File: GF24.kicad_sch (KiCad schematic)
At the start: 52 parts, among them J1 Conn_02x05_Odd_Even, J2 USB_C_Receptacle_PowerOnly_6P, Q1 MMBT3904LT1G, SW1 NRST, SW2 SW_Nidec_CAS-120A1, SW3 NRST, SW4 ON/OFF, SW5 MODE, U1 STM32F031C4T6, U2 SAM-M10Q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

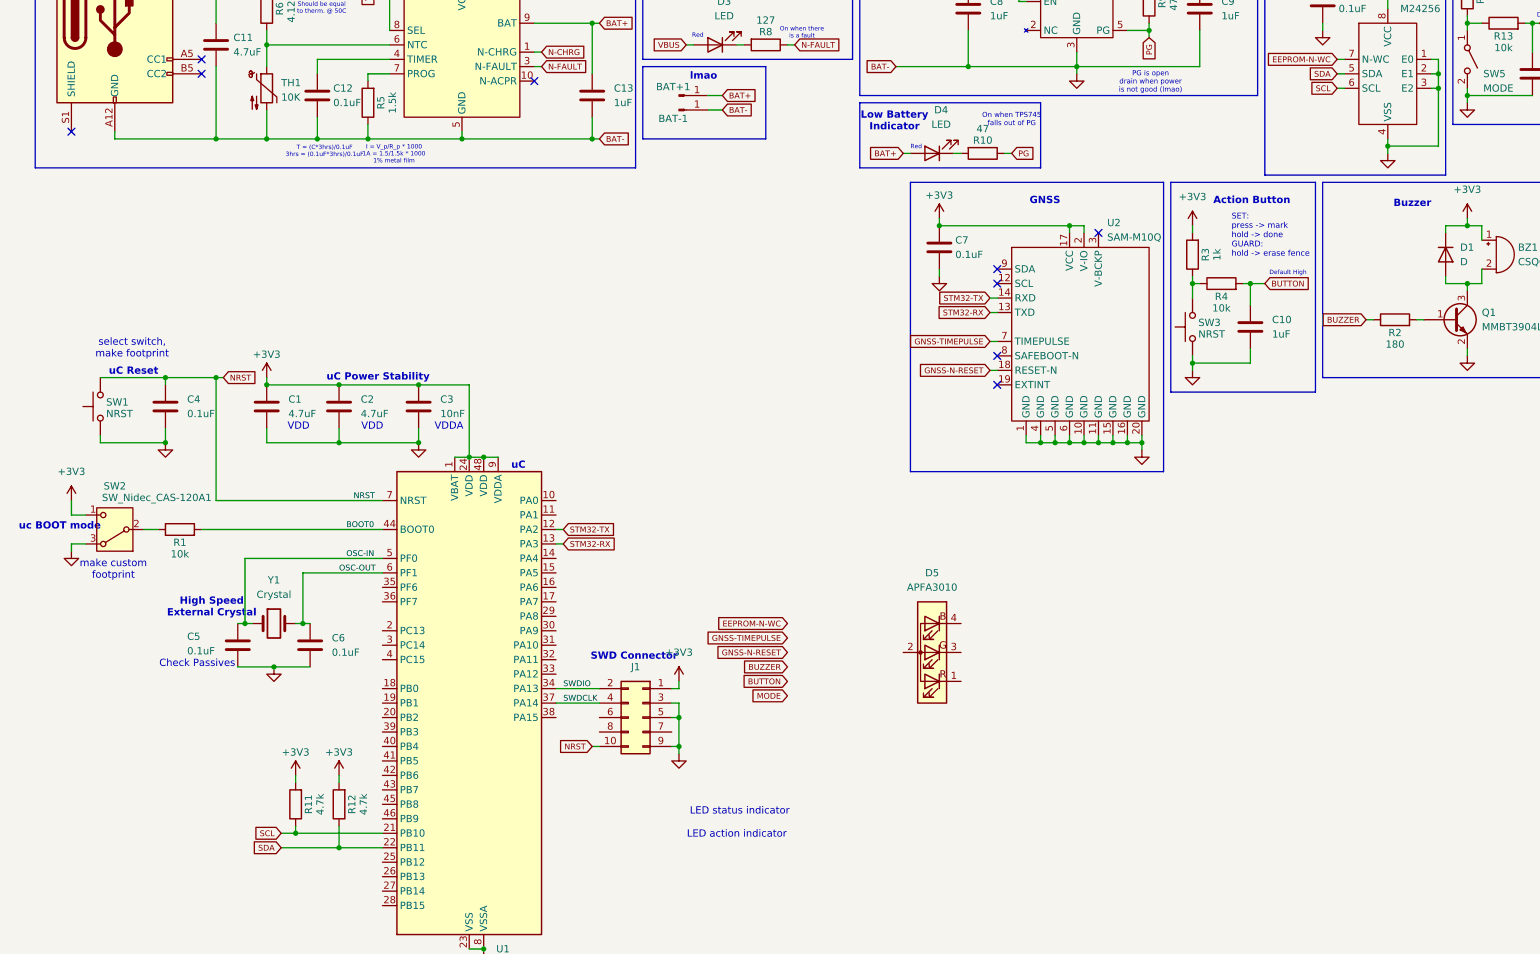
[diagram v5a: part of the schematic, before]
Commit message: added status LEDs
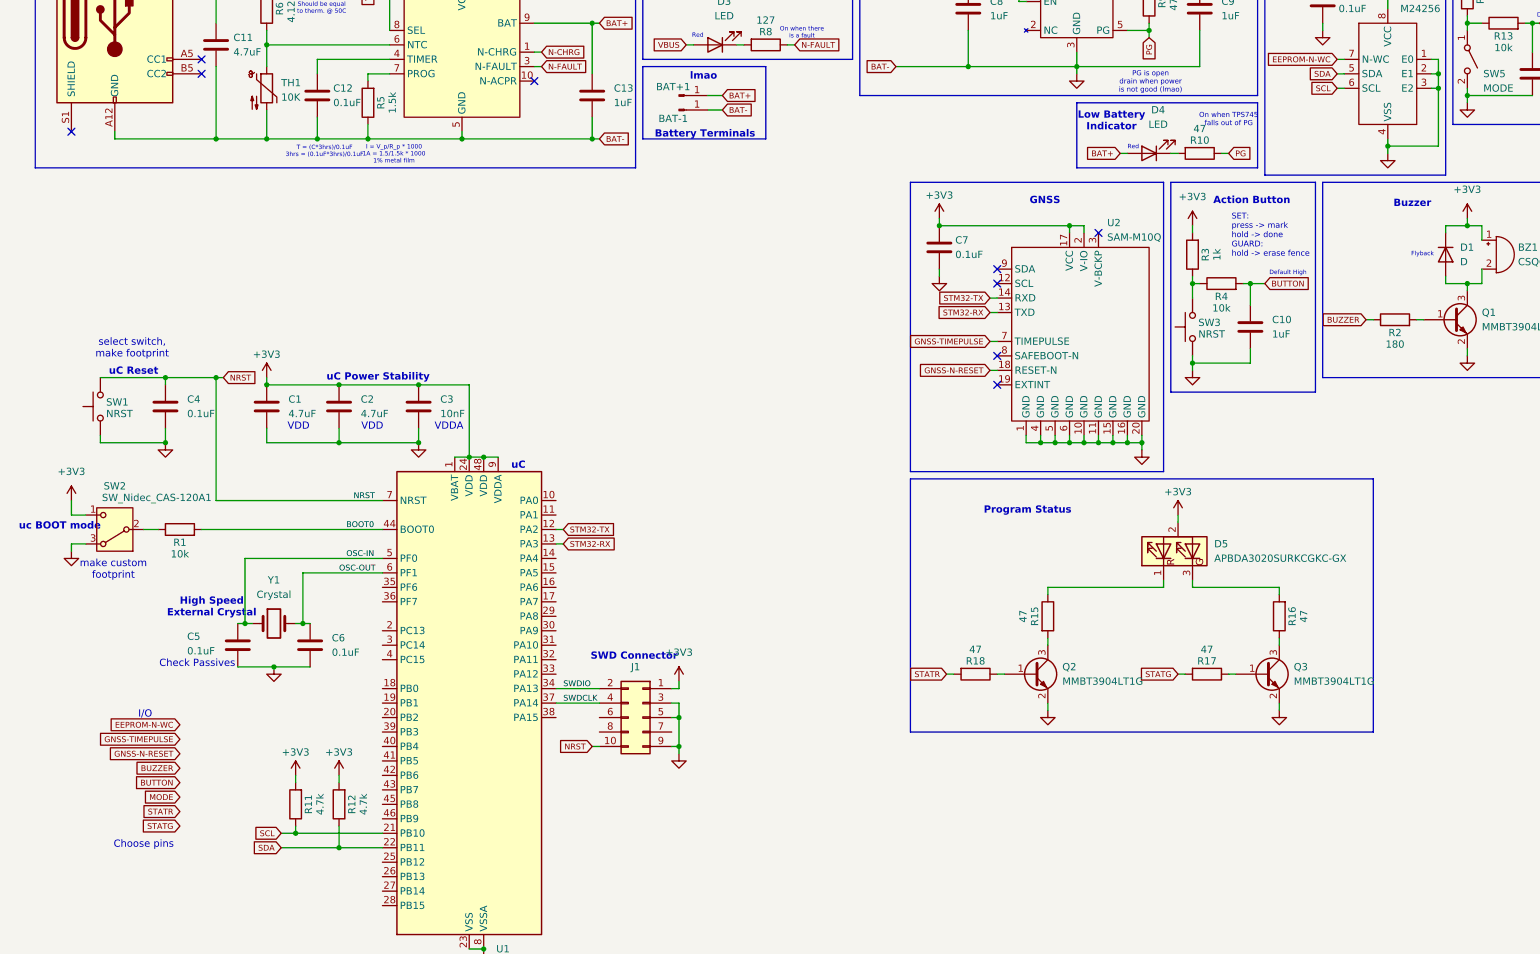
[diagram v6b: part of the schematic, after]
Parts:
- removed D5: APFA3010, LED_SMD:LED_Kingbright_APFA3010_3x1.5mm_Horizontal, symbol LED:APFA3010
- added D5: APBDA3020SURKCGKC-GX, symbol MB-Opto:APBDA3020SURKCGKC-GX
- added Q2, Q3: MMBT3904LT1G, MB-SOT:SOT-23-3, symbol Transistor_BJT:2SC4213
- added R15, R16, R17, R18: 47, MB-Generic:R1206_medium, symbol Device:R
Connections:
- net +3V3: now also D5.2 (A)
- net GND: now also Q2.2 (E), Q3.2 (E)
- new net: D5.1 (R), R15.1
- new net: Q2.3 (C), R15.2
- new net: D5.3 (G), R16.2
- new net: Q3.1 (B), R17.1
- new net: Q3.3 (C), R16.1
- new net: Q2.1 (B), R18.1
- new net STATG: R17.2
- new net STATR: R18.2
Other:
- note added: "Battery Terminals"
- note added: "Choose pins"
- note added: "Flyback"
- note added: "I/O"
- note added: "Program Status"
- note removed: "LED action indicator"
- note removed: "LED status indicator"
- moved on the sheet: D4, R10

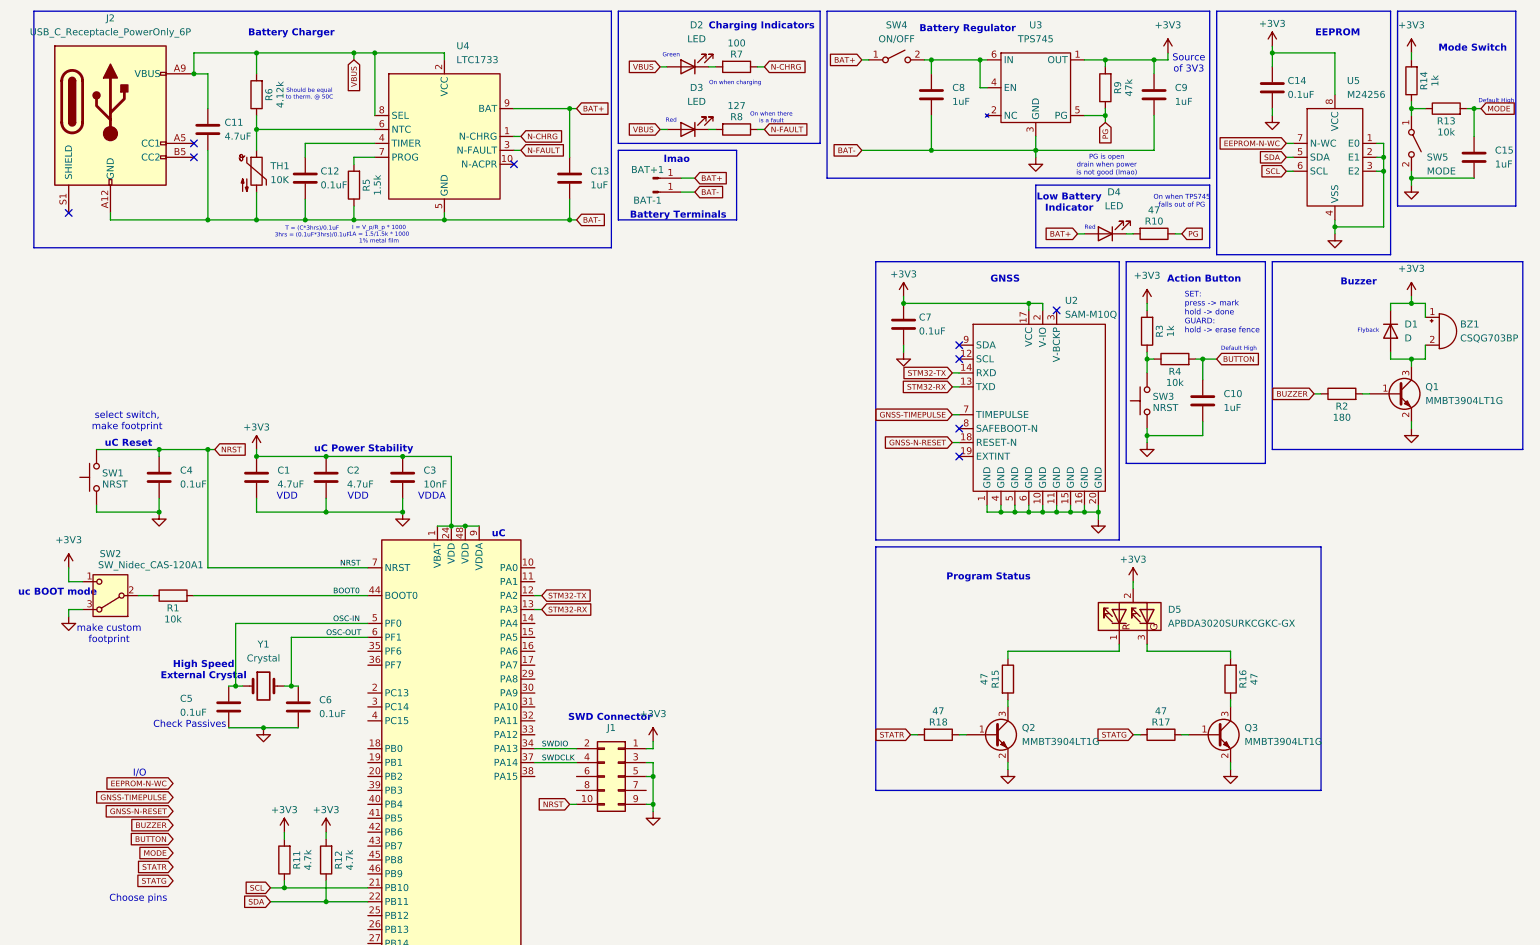
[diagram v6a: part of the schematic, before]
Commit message: fixed PG indicator, grouped parts functionally
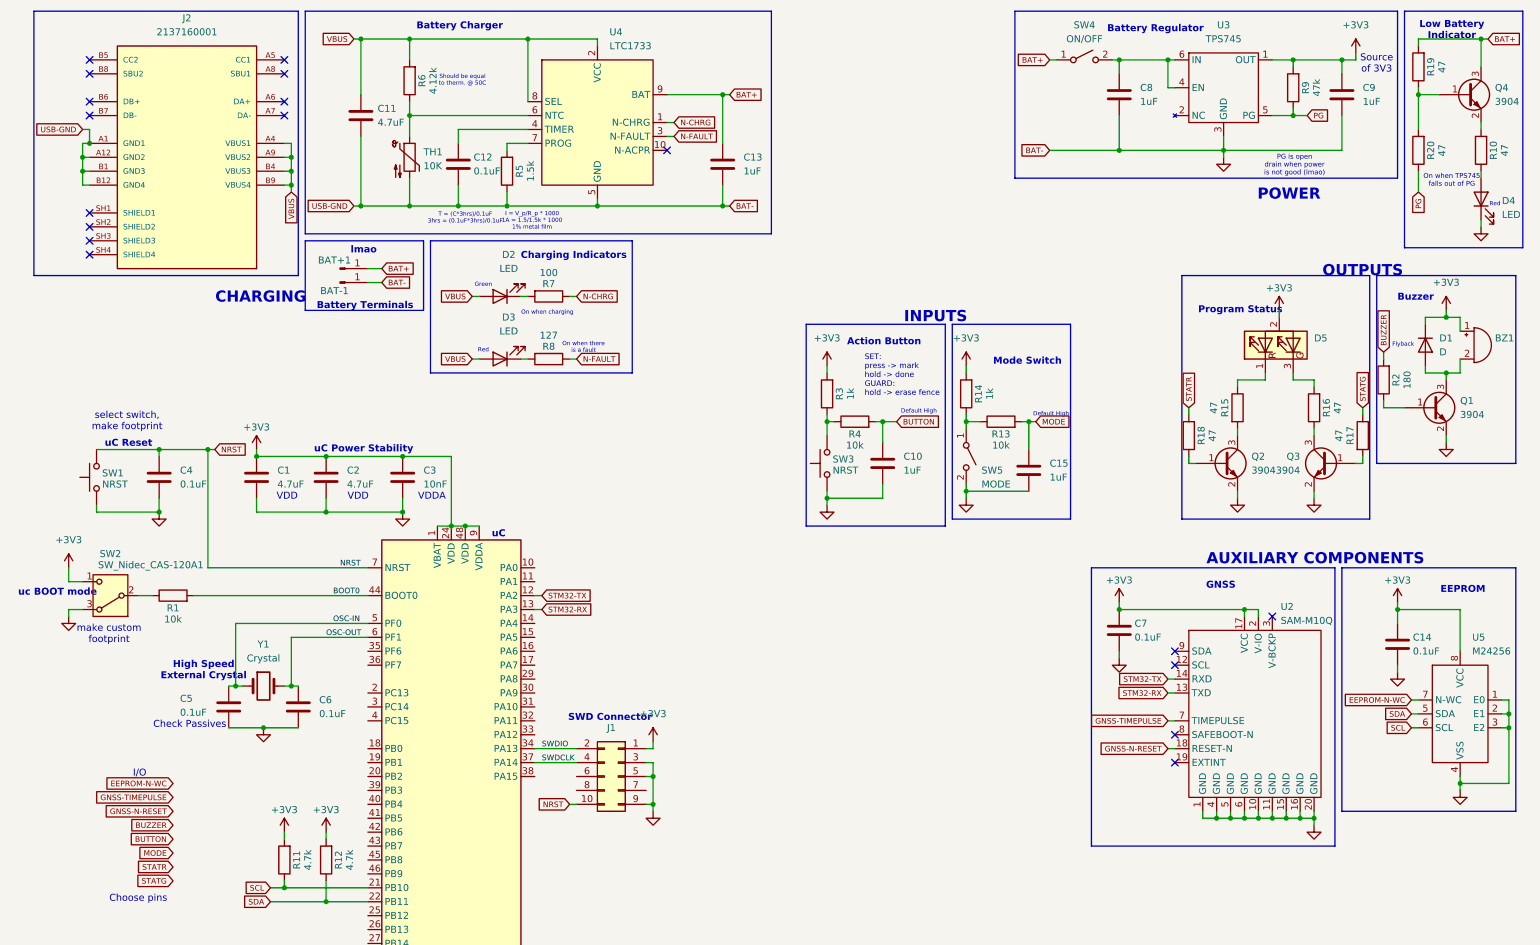
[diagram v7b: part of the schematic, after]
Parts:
- added Q4: 3904, MB-SOT:SOT-23-3, symbol Transistor_BJT:2SC4213
- added R19, R20: 47, MB-Generic:R1206_medium, symbol Device:R
- J2: value USB_C_Receptacle_PowerOnly_6P -> 2137160001; footprint (none) -> 2137160001:MOLEX_2137160001; symbol Connector:USB_C_Receptacle_PowerOnly_6P -> 2137160001:2137160001; MANUFACTURER (none) -> Molex; MAXIMUM_PACKAGE_HEIGHT (none) -> 3.36mm; OPTION (none) -> MOLEX_CONFIG; PARTREV (none) -> B; STANDARD (none) -> Manufacturer Recommendations
- Q1, Q2, Q3: value MMBT3904LT1G -> 3904
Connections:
- net BAT+: now also Q4.3 (C), R19.2; no longer D4.2 (A)
- net BUZZER: now also R2.2; no longer R2.1
- net GND: now also D4.1 (K), J2.A1 (GND1), J2.B1 (GND3)
- net PG: now also R20.1; no longer R10.1
- net STATG: now also R17.1; no longer R17.2
- net VBUS: now also J2.A4 (VBUS1), J2.B4 (VBUS3)
- net at Q1.1 (B): now also R2.1; no longer R2.2
- net at Q3.1 (B): now also R17.2; no longer R17.1
- net at R10.2: now also Q4.2 (E); no longer D4.1 (K)
- new net: Q4.1 (B), R19.1, R20.2
- new net: D4.2 (A), R10.1
- no-connect marks 9 -> 18
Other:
- note added: "AUXILIARY COMPONENTS"
- note added: "CHARGING"
- note added: "INPUTS"
- note added: "OUTPUTS"
- note added: "POWER"
- moved on the sheet: BAT+1, BAT-1, BZ1, C10, C11, C12, C13, C14, C15, C7, C8, C9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

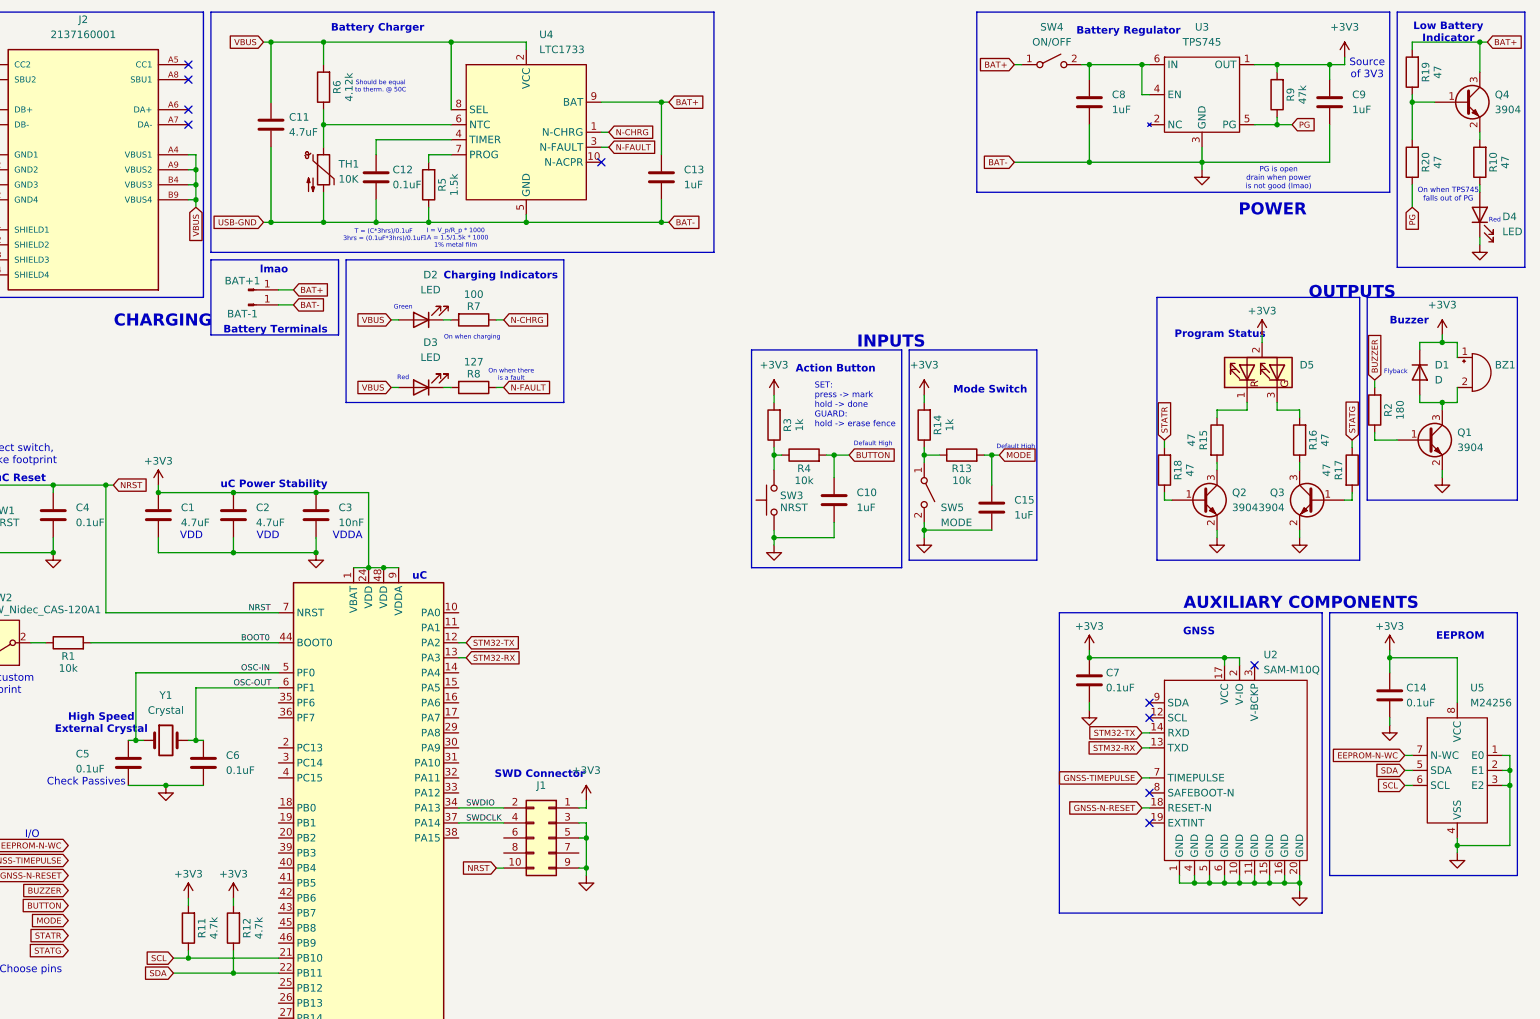
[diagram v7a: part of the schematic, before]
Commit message: changed most LED circuits which deal with open drain outputs
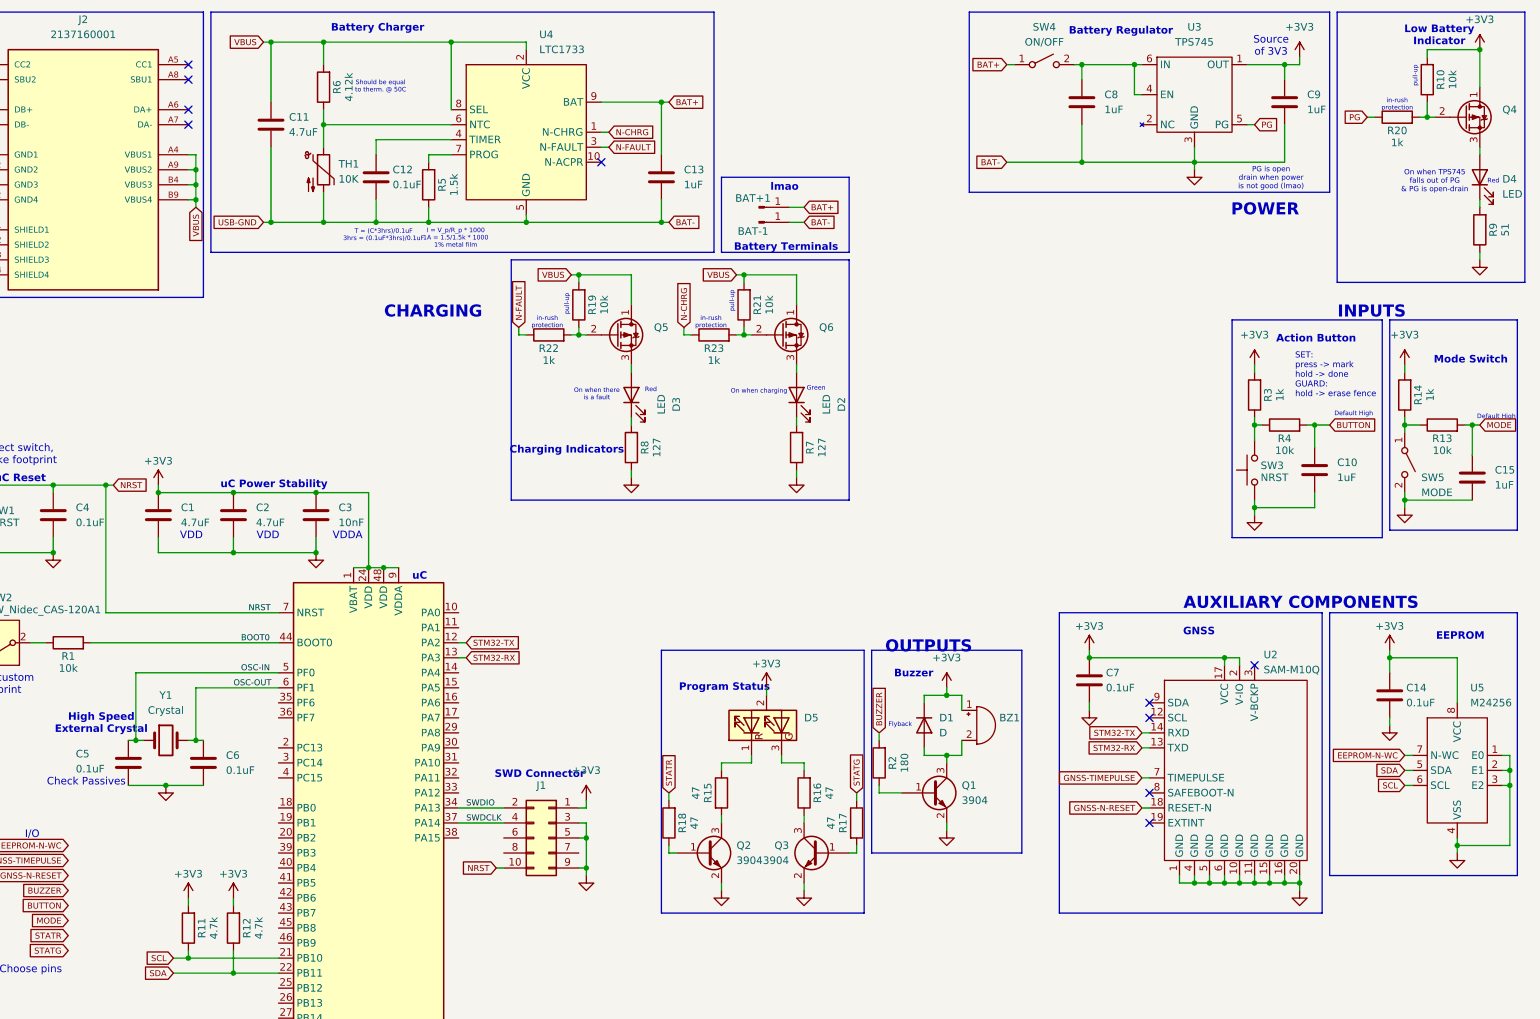
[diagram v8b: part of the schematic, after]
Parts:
- removed Q4: 3904, MB-SOT:SOT-23-3, symbol Transistor_BJT:2SC4213
- added Q4, Q5, Q6: DMP2004K-7, symbol Device:Q_PMOS_DGS
- added R21: 10k, MB-Generic:R1206_medium, symbol Device:R
- added R22, R23: 1k, MB-Generic:R1206_medium, symbol Device:R
- R10, R19: value 47 -> 10k
- R20: value 47 -> 1k
- R7: value 100 -> 127
- R9: value 47k -> 51
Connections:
- net +3V3: now also R10.2, Q4.1 (D); no longer R9.2
- net BAT+: no longer R19.2
- net GND: now also R7.1, R8.1, R9.1; no longer D4.1 (K)
- net N-CHRG: now also R23.1; no longer R7.1
- net N-FAULT: now also R22.1; no longer R8.1
- net PG: no longer R9.1
- net VBUS: now also R19.2, Q5.1 (D), Q6.1 (D), R21.2; no longer D2.2 (A), D3.2 (A)
- net at R19.1: now also Q5.2 (G), R22.2; no longer R20.2
- net at R10.1: now also R20.2, Q4.2 (G); no longer D4.2 (A)
- new net: Q6.2 (G), R21.1, R23.2
- new net: D4.2 (A), Q4.3 (S)
- new net: D3.2 (A), Q5.3 (S)
- new net: D2.2 (A), Q6.3 (S)
- new net: D4.1 (K), R9.2
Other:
- note added: "On when TPS745 falls out of PG & PG is open-drain"
- note added: "in-rush protection"
- note added: "pull-up"
- note removed: "On when TPS745 falls out of PG"
- moved on the sheet: BAT+1, BAT-1, BZ1, C10, C15, C8, C9, D1, D2, D3, D4, D5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
